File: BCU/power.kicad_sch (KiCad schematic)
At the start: 28 parts

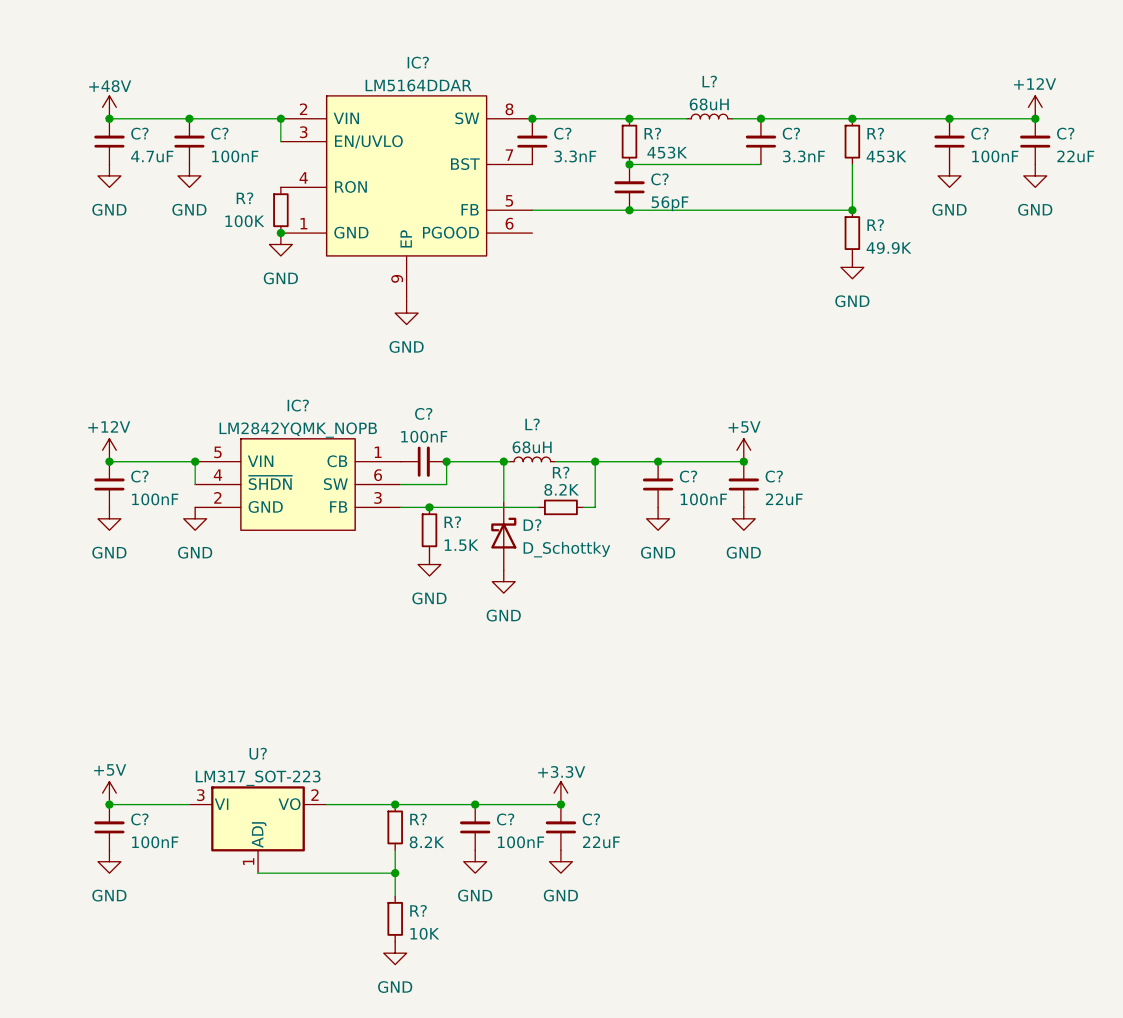
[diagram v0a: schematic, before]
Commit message: Make rough component placement for evaluating missing 3D
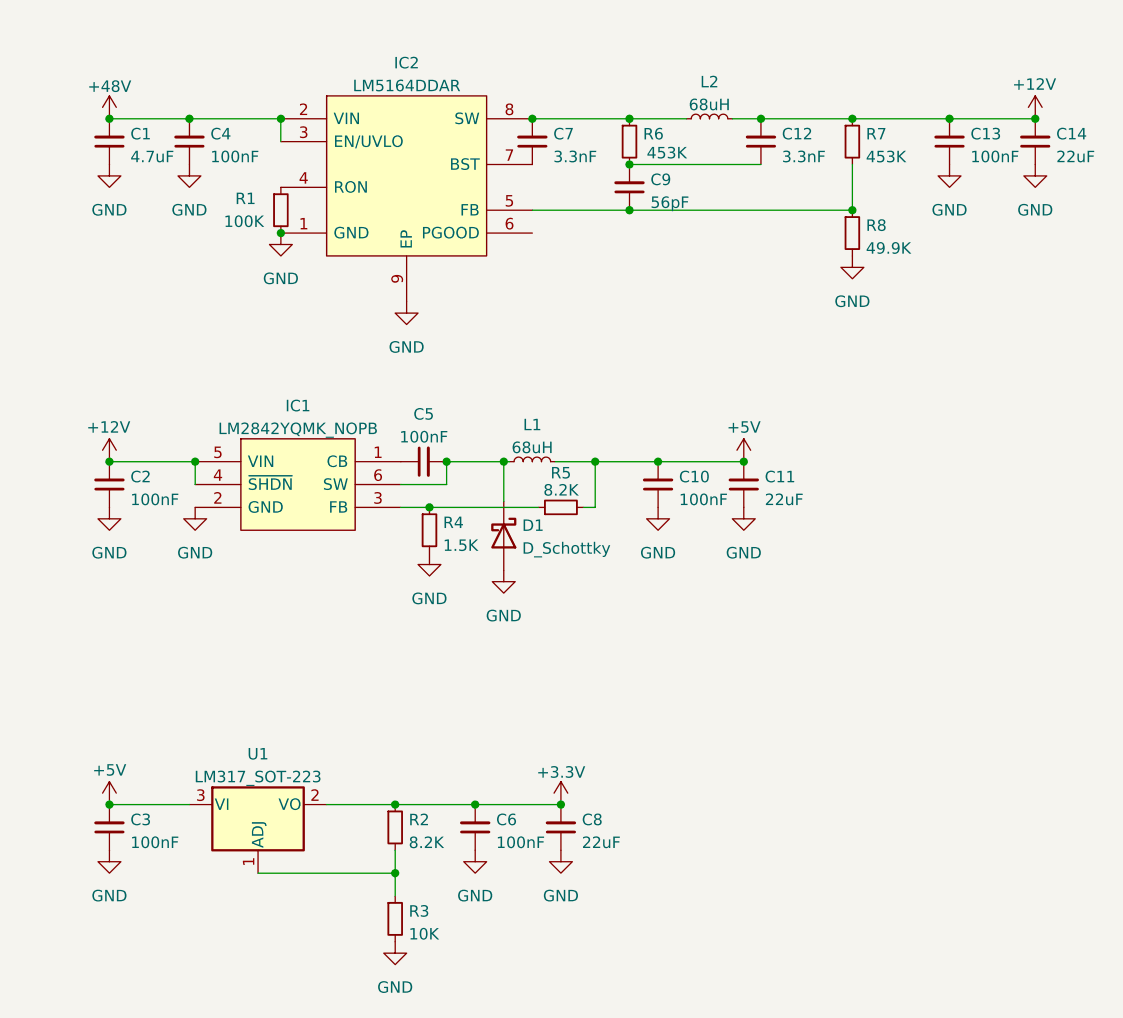
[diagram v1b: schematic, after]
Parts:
- removed IC?: LM5164DDAR, SOIC127P600X170-9N, symbol coilchain-power:LM5164DDAR
- removed IC?: LM2842YQMK_NOPB, SOT95P280X110-6N, symbol coilchain-power:LM2842YQMK_NOPB
- added IC1: LM2842YQMK_NOPB, Package_TO_SOT_SMD:SuperSOT-6, symbol coilchain-power:LM2842YQMK_NOPB
- added IC2: LM5164DDAR, Package_SO:Texas_R-PDSO-G8_EP2.95x4.9mm_Mask2.4x3.1mm_ThermalVias, symbol coilchain-power:LM5164DDAR
- gave numbers to parts that had none: 26
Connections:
- net +12V: now also IC1.4 (~{SHDN}), IC1.5 (VIN)
- net +48V: now also IC2.2 (VIN), IC2.3 (EN/UVLO)
- net GND: now also IC1.2 (GND), IC2.1 (GND), IC2.9 (EP)
- net at R1.1: now also IC2.4 (RON)
- net at C5.2, D1.1 (K), L1.1: now also IC1.6 (SW)
- net at C7.1: now also IC2.7 (BST)
- net at C7.2, L2.1, R6.1: now also IC2.8 (SW)
- net at C5.1: now also IC1.1 (CB)
- net at R4.1, R5.1: now also IC1.3 (FB)
- net at C9.1, R7.2, R8.1: now also IC2.5 (FB)

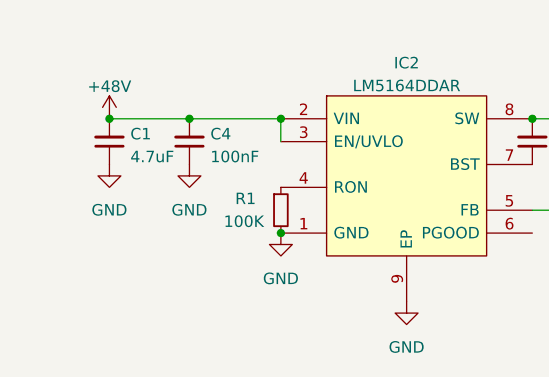
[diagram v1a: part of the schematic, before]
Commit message: change 48v to +BATT, increase cap sizes
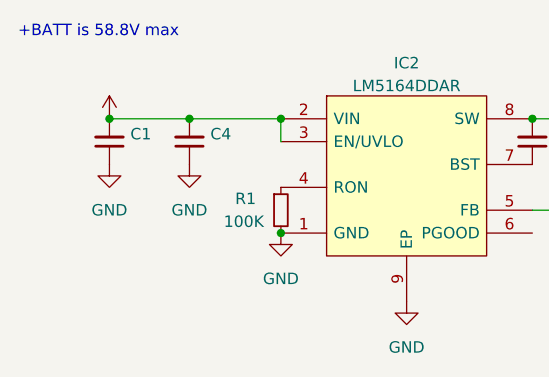
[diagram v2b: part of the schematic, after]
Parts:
- C1: value 4.7uF -> (none); footprint Capacitor_SMD:C_0603_1608Metric_Pad1.08x0.95mm_HandSolder -> (none)
- C4: value 100nF -> (none); footprint Capacitor_SMD:C_0402_1005Metric_Pad0.74x0.62mm_HandSolder -> (none)
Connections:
- net +48V renamed +BATT
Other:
- note added: "+BATT is 58.8V max"
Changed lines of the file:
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@@
   (junction (at 92.075 95.25) (diameter 0) (color 0 0 0 0)
   )
+  (junction (at 38.1 57.15) (diameter 0) (color 0 0 0 0)
+  )
   (junction (at 57.15 69.85) (diameter 0) (color 0 0 0 0)
   )
@@
   (junction (at 95.885 57.15) (diameter 0) (color 0 0 0 0)
   )
-  (junction (at 38.1 57.15) (diameter 0) (color 0 0 0 0)
-  )
   (junction (at 69.85 133.35) (diameter 0) (color 0 0 0 0)
   )
@@
   (wire (pts (xy 38.1 133.35) (xy 46.99 133.35))
     (stroke (width 0) (type default) (color 0 0 0 0))
+  )
+  (text "+BATT is 58.8V max" (at 27.94 48.26 0)
+    (effects (font (size 1.27 1.27)) (justify left bottom))
   )
   (symbol (lib_id "power:+12V") (at 140.97 57.15 0) (unit 1)
@@
       (effects (font (size 1.27 1.27)) (justify right))
     )
-    (property "Value" "100nF" (id 1) (at 49.3141 61.3858 0)
-      (effects (font (size 1.27 1.27)) (justify right))
-    )
-    (property "Footprint" "Capacitor_SMD:C_0402_1005Metric_Pad0.74x0.62mm_HandSolder" (id 2) (at 46.99 59.69 0)
+    (property "Value" "" (id 1) (at 49.3141 61.3858 0)
+      (effects (font (size 1.27 1.27)) (justify right))
+    )
+    (property "Footprint" "" (id 2) (at 46.99 59.69 0)
       (effects (font (size 1.27 1.27)) hide)
     )
@@
     (pin "1")
     (pin "2")
-  )
-  (symbol (lib_id "power:+48V") (at 38.1 57.15 0) (unit 1)
-    (in_bom yes) (on_board yes) (fields_autoplaced)
-    (property "Reference" "#PWR0119" (id 0) (at 38.1 60.96 0)
-      (effects (font (size 1.27 1.27)) hide)
-    )
-    (property "Value" "+48V" (id 1) (at 38.1 53.5742 0))
-    (property "Footprint" "" (id 2) (at 38.1 57.15 0)
-      (effects (font (size 1.27 1.27)) hide)
-    )
-    (property "Datasheet" "" (id 3) (at 38.1 57.15 0)
-      (effects (font (size 1.27 1.27)) hide)
-    )
-    (pin "1")
   )
   (symbol (lib_id "power:GND") (at 38.1 62.23 0) (unit 1)
@@
     (pin "1")
   )
+  (symbol (lib_id "power:+BATT") (at 38.1 57.15 0) (unit 1)
+    (in_bom yes) (on_board yes) (fields_autoplaced)
+    (property "Reference" "#PWR?" (id 0) (at 38.1 60.96 0)
+      (effects (font (size 1.27 1.27)) hide)
+    )
+    (property "Value" "" (id 1) (at 38.1 52.07 0))
+    (property "Footprint" "" (id 2) (at 38.1 57.15 0)
+      (effects (font (size 1.27 1.27)) hide)
+    )
+    (property "Datasheet" "" (id 3) (at 38.1 57.15 0)
+      (effects (font (size 1.27 1.27)) hide)
+    )
+    (pin "1")
+  )
   (symbol (lib_id "Device:R_Small") (at 69.85 146.05 0) (unit 1)
     (in_bom yes) (on_board yes) (fields_autoplaced)
@@
       (effects (font (size 1.27 1.27)) (justify right))
     )
-    (property "Value" "4.7uF" (id 1) (at 40.4241 61.3858 0)
-      (effects (font (size 1.27 1.27)) (justify right))
-    )
-    (property "Footprint" "Capacitor_SMD:C_0603_1608Metric_Pad1.08x0.95mm_HandSolder" (id 2) (at 38.1 59.69 0)
-      (effects (font (size 1.27 1.27)) hide)
-    )
+    (property "Value" "" (id 1) (at 40.4241 61.3858 0)
+      (effects (font (size 1.27 1.27)) (justify right))
+    )
+    (property "Footprint" "" (id 2) (at 38.1 59.69 0)
+      (effects (font (size 1.27 1.27)) hide)
+    )

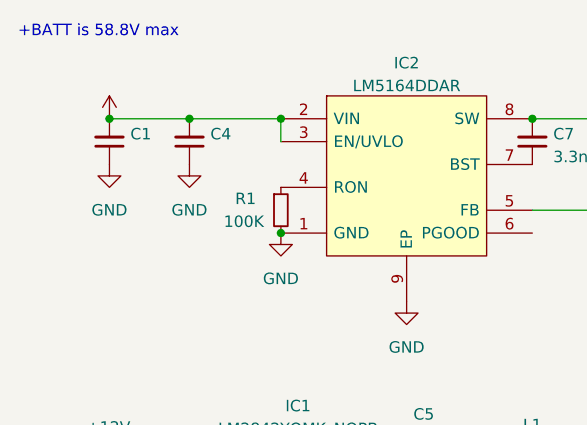
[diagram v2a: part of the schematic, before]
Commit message: Added power enable logic
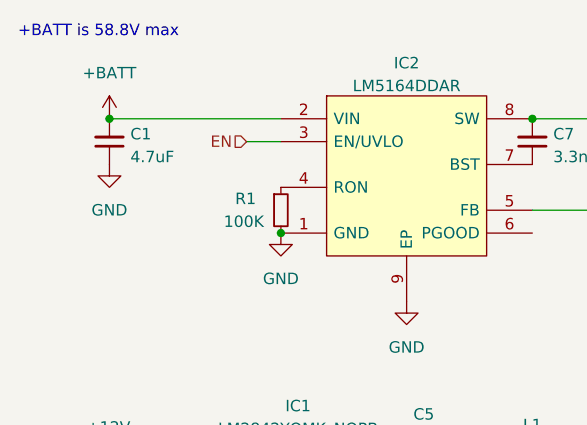
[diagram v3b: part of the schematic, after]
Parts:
- removed C4: (no value), symbol Device:C_Small
- C1: value (none) -> 4.7uF; footprint (none) -> Capacitor_SMD:C_1206_3216Metric
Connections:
- net +BATT: no longer IC2.3 (EN/UVLO)
- new net EN: IC2.3 (EN/UVLO)
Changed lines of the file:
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@@
   (junction (at 73.66 100.33) (diameter 0) (color 0 0 0 0)
   )
-  (junction (at 46.99 57.15) (diameter 0) (color 0 0 0 0)
-  )
-  (junction (at 57.15 57.15) (diameter 0) (color 0 0 0 0)
-  )
   (junction (at 47.625 95.25) (diameter 0) (color 0 0 0 0)
   )
@@
     (stroke (width 0) (type default) (color 0 0 0 0))
   )
-  (wire (pts (xy 46.99 57.15) (xy 57.15 57.15))
+  (wire (pts (xy 38.1 57.15) (xy 57.15 57.15))
     (stroke (width 0) (type default) (color 0 0 0 0))
   )
@@
     (stroke (width 0) (type default) (color 0 0 0 0))
   )
-  (wire (pts (xy 38.1 57.15) (xy 46.99 57.15))
-    (stroke (width 0) (type default) (color 0 0 0 0))
-  )
   (wire (pts (xy 54.61 140.97) (xy 69.85 140.97))
     (stroke (width 0) (type default) (color 0 0 0 0))
@@
     (stroke (width 0) (type default) (color 0 0 0 0))
   )
-  (wire (pts (xy 57.15 57.15) (xy 57.15 59.69))
-    (stroke (width 0) (type default) (color 0 0 0 0))
-  )
   (wire (pts (xy 99.06 95.25) (xy 108.585 95.25))
+    (stroke (width 0) (type default) (color 0 0 0 0))
+  )
+  (wire (pts (xy 53.34 59.69) (xy 57.15 59.69))
     (stroke (width 0) (type default) (color 0 0 0 0))
   )
@@
   (text "+BATT is 58.8V max" (at 27.94 48.26 0)
     (effects (font (size 1.27 1.27)) (justify left bottom))
+  )
+  (hierarchical_label "EN" (shape input) (at 53.34 59.69 180)
+    (effects (font (size 1.27 1.27)) (justify right))
   )
   (symbol (lib_id "power:+12V") (at 140.97 57.15 0) (unit 1)
@@
     (pin "1")
   )
-  (symbol (lib_id "Device:C_Small") (at 46.99 59.69 180) (unit 1)
-    (in_bom yes) (on_board yes) (fields_autoplaced)
-    (property "Reference" "C4" (id 0) (at 49.3141 58.8489 0)
-      (effects (font (size 1.27 1.27)) (justify right))
-    )
-    (property "Value" "" (id 1) (at 49.3141 61.3858 0)
-      (effects (font (size 1.27 1.27)) (justify right))
-    )
-    (property "Footprint" "" (id 2) (at 46.99 59.69 0)
-      (effects (font (size 1.27 1.27)) hide)
-    )
-    (property "Datasheet" "~" (id 3) (at 46.99 59.69 0)
-      (effects (font (size 1.27 1.27)) hide)
-    )
-    (pin "1")
-    (pin "2")
-  )
   (symbol (lib_id "power:GND") (at 131.445 62.23 0) (unit 1)
     (in_bom yes) (on_board yes) (fields_autoplaced)
@@
     (pin "2")
   )
-  (symbol (lib_id "power:GND") (at 46.99 62.23 0) (unit 1)
-    (in_bom yes) (on_board yes) (fields_autoplaced)
-    (property "Reference" "#PWR0118" (id 0) (at 46.99 68.58 0)
-      (effects (font (size 1.27 1.27)) hide)
-    )
-    (property "Value" "GND" (id 1) (at 46.99 67.31 0))
-    (property "Footprint" "" (id 2) (at 46.99 62.23 0)
-      (effects (font (size 1.27 1.27)) hide)
-    )
-    (property "Datasheet" "" (id 3) (at 46.99 62.23 0)
-      (effects (font (size 1.27 1.27)) hide)
-    )
-    (pin "1")
-  )
   (symbol (lib_id "Device:C_Small") (at 110.49 59.69 180) (unit 1)
     (in_bom yes) (on_board yes) (fields_autoplaced)
@@
       (effects (font (size 1.27 1.27)) hide)
     )
-    (property "Value" "" (id 1) (at 38.1 52.07 0))
+    (property "Value" "+BATT" (id 1) (at 38.1 52.07 0))
     (property "Footprint" "" (id 2) (at 38.1 57.15 0)
       (effects (font (size 1.27 1.27)) hide)
@@
       (effects (font (size 1.27 1.27)) (justify right))
     )
-    (property "Value" "" (id 1) (at 40.4241 61.3858 0)
-      (effects (font (size 1.27 1.27)) (justify right))
-    )
-    (property "Footprint" "" (id 2) (at 38.1 59.69 0)
-      (effects (font (size 1.27 1.27)) hide)
-    )
+    (property "Value" "4.7uF" (id 1) (at 40.4241 61.3858 0)
+      (effects (font (size 1.27 1.27)) (justify right))
+    )
+    (property "Footprint" "Capacitor_SMD:C_1206_3216Metric" (id 2) (at 38.1 59.69 0)
+      (effects (font (size 1.27 1.27)) hide)
+    )
